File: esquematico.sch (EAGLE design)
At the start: 15 parts, among them IC1 TS321IDBVR, IC2 ESP32-S3-WROOM-1-N16R8, IC3 MAX30102EFD+T

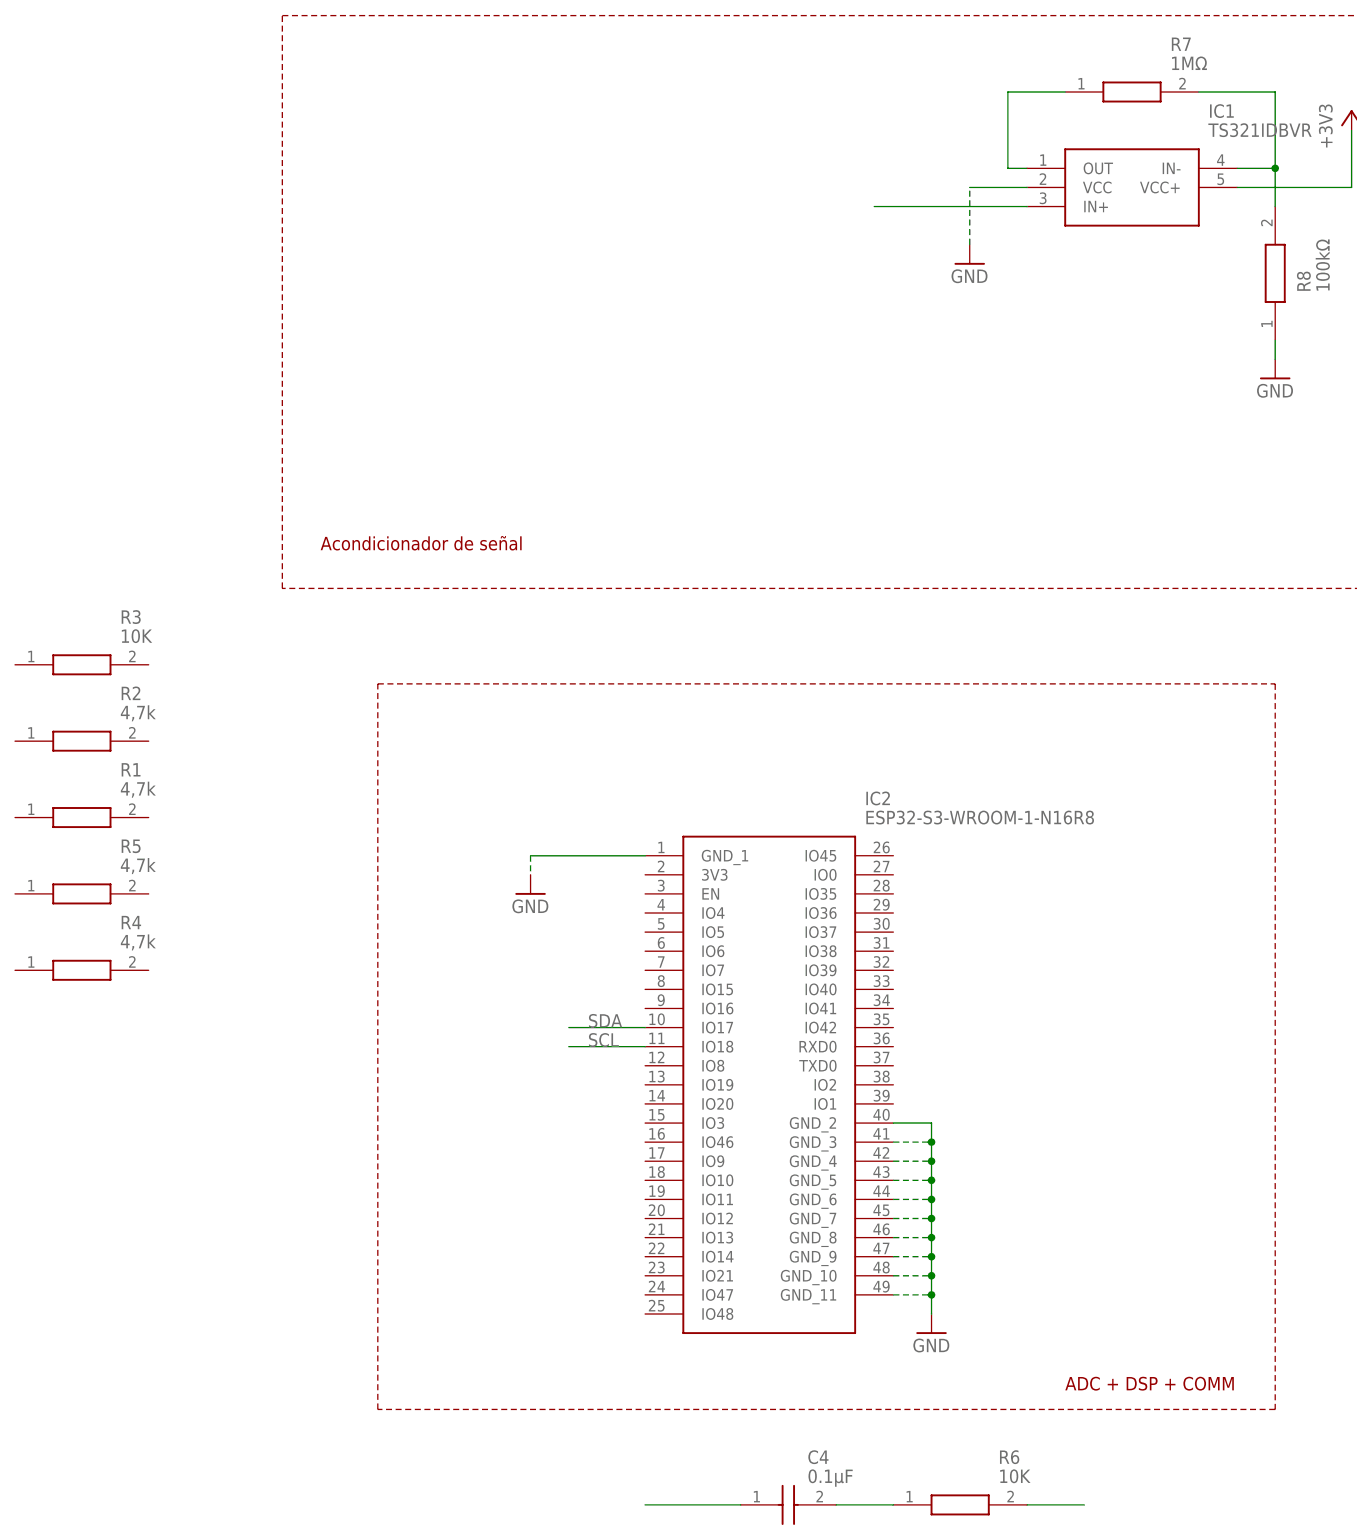
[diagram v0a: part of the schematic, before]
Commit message: Finalizado Bloque 1: Acondicionador de señal
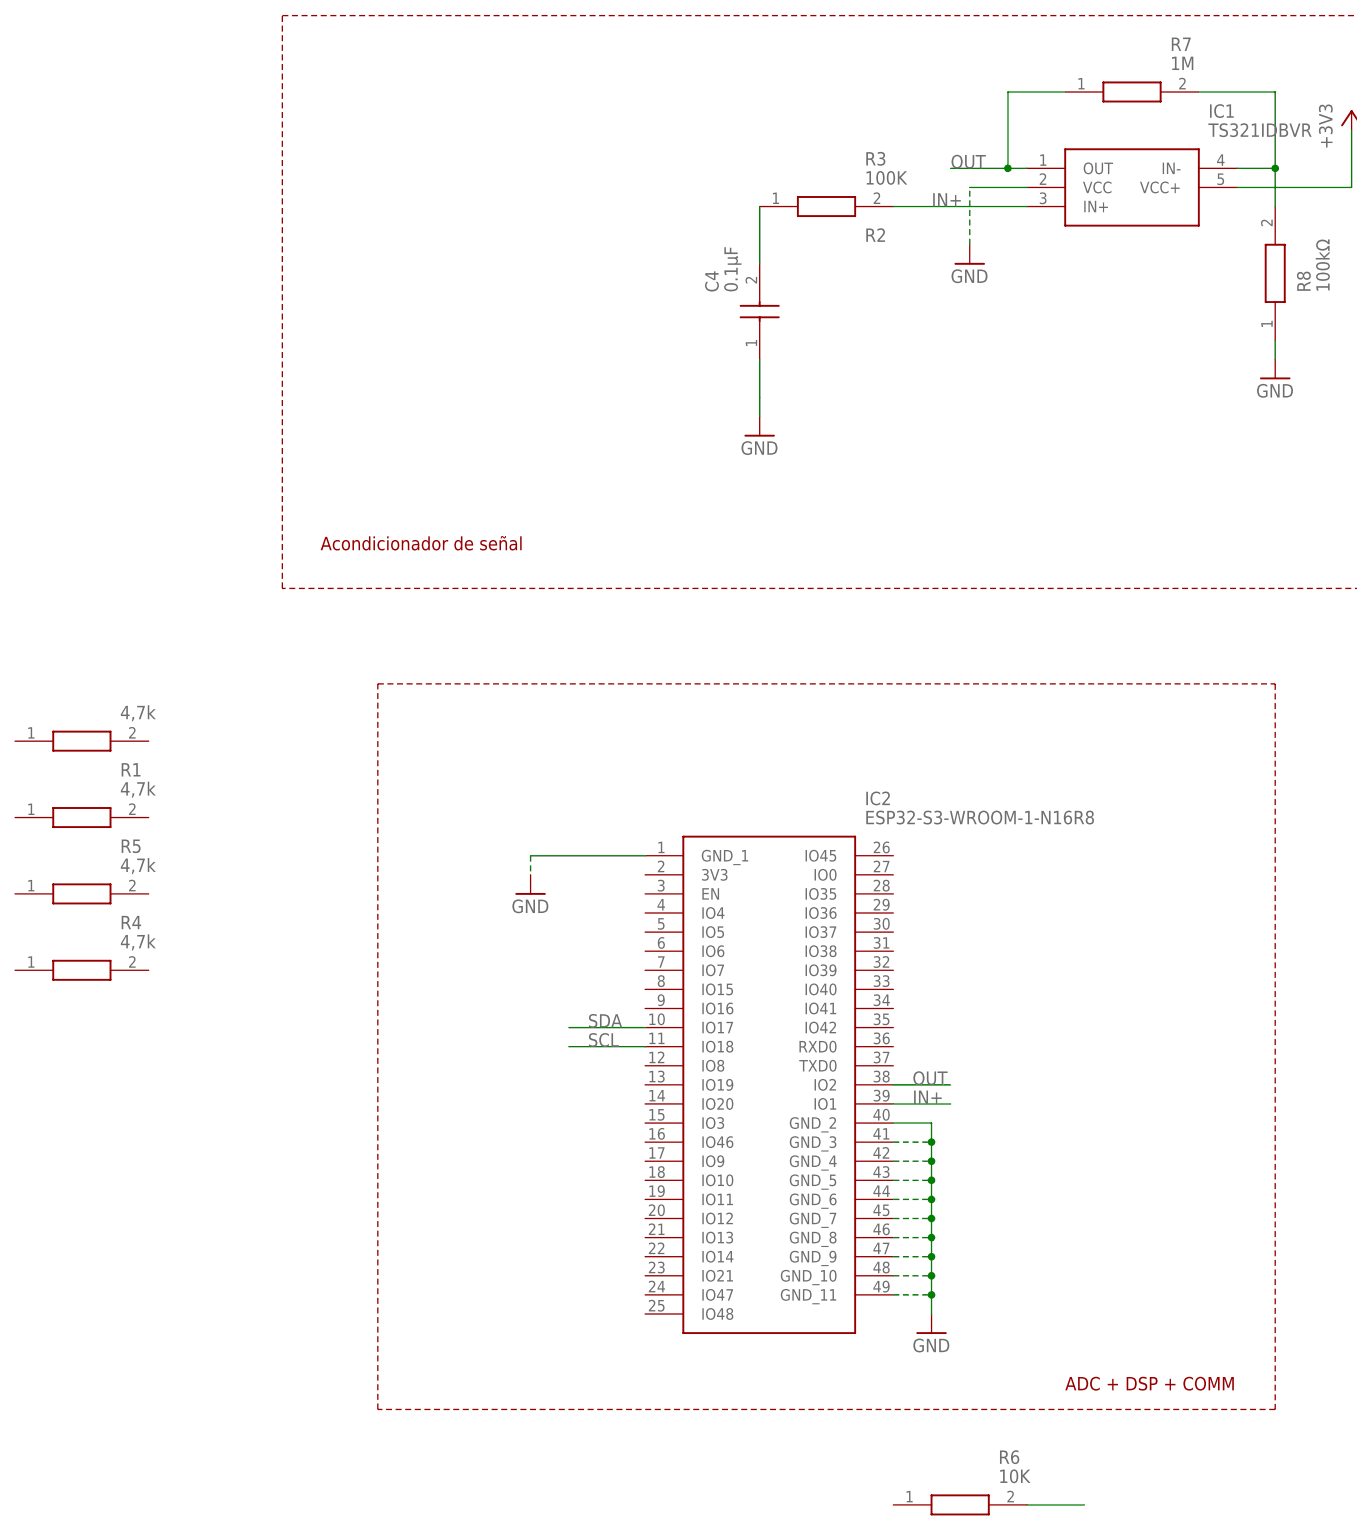
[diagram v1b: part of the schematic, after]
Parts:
- R3: value 10K -> 100K
- R7: value 1MΩ -> 1M
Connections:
- removed net N$11: IC1.IN+
- removed net N$12: C4.2, R6.1
- removed net N$14: IC1.OUT, R7.1
- new net IN+: IC1.IN+, IC2.IO1, R3.2
- new net N$1: C4.2, R3.1
- new net OUT: IC1.OUT, IC2.IO2, R7.1
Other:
- moved on the sheet: C4, R3
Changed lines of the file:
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@@
 <part name="R2" library="0805S8F1202P5E" deviceset="0805S8F1202P5E" device="" value="4,7k"/>
 <part name="R1" library="0805S8F1202P5E" deviceset="0805S8F1202P5E" device="" value="4,7k"/>
-<part name="R3" library="0805S8F1202P5E" deviceset="0805S8F1202P5E" device="" value="10K"/>
+<part name="R3" library="0805S8F1202P5E" deviceset="0805S8F1202P5E" device="" value="100K"/>
 <part name="R4" library="0805S8F1202P5E" deviceset="0805S8F1202P5E" device="" value="4,7k"/>
 <part name="R5" library="0805S8F1202P5E" deviceset="0805S8F1202P5E" device="" value="4,7k"/>
@@
 <part name="R6" library="0805S8F1202P5E" deviceset="0805S8F1202P5E" device="" value="10K"/>
 <part name="C4" library="C0805J104K1RACAUTO" deviceset="C0805J104K1RACAUTO" device="" value="0.1µF"/>
-<part name="R7" library="0805S8F1202P5E" deviceset="0805S8F1202P5E" device="" value="1MΩ"/>
+<part name="R7" library="0805S8F1202P5E" deviceset="0805S8F1202P5E" device="" value="1M"/>
 <part name="R8" library="0805S8F1202P5E" deviceset="0805S8F1202P5E" device="" value="100kΩ"/>
 <part name="+3V1" library="supply1" library_urn="urn:adsk.eagle:library:371" deviceset="+3V3" device=""/>
@@
 <part name="GND6" library="supply1" library_urn="urn:adsk.eagle:library:371" deviceset="GND" device=""/>
 <part name="GND7" library="supply1" library_urn="urn:adsk.eagle:library:371" deviceset="GND" device=""/>
+<part name="GND8" library="supply1" library_urn="urn:adsk.eagle:library:371" deviceset="GND" device=""/>
 </parts>
 <sheets>
@@
 </instance>
 <instance part="R2" gate="G$1" x="76.2" y="142.24" smashed="yes">
-<attribute name="NAME" x="90.17" y="148.59" size="1.778" layer="95" align="center-left"/>
+<attribute name="NAME" x="189.23" y="209.55" size="1.778" layer="95" align="center-left"/>
 <attribute name="VALUE" x="90.17" y="146.05" size="1.778" layer="96" align="center-left"/>
 </instance>
@@
 <attribute name="VALUE" x="90.17" y="135.89" size="1.778" layer="96" align="center-left"/>
 </instance>
-<instance part="R3" gate="G$1" x="76.2" y="152.4" smashed="yes">
-<attribute name="NAME" x="90.17" y="158.75" size="1.778" layer="95" align="center-left"/>
-<attribute name="VALUE" x="90.17" y="156.21" size="1.778" layer="96" align="center-left"/>
+<instance part="R3" gate="G$1" x="175.26" y="213.36" smashed="yes">
+<attribute name="NAME" x="189.23" y="219.71" size="1.778" layer="95" align="center-left"/>
+<attribute name="VALUE" x="189.23" y="217.17" size="1.778" layer="96" align="center-left"/>
 </instance>
 <instance part="R4" gate="G$1" x="76.2" y="111.76" smashed="yes">
@@
 <attribute name="VALUE" x="207.01" y="44.45" size="1.778" layer="96" align="center-left"/>
 </instance>
-<instance part="C4" gate="G$1" x="172.72" y="40.64" smashed="yes">
-<attribute name="NAME" x="181.61" y="46.99" size="1.778" layer="95" align="center-left"/>
-<attribute name="VALUE" x="181.61" y="44.45" size="1.778" layer="96" align="center-left"/>
+<instance part="C4" gate="G$1" x="175.26" y="193.04" smashed="yes" rot="R90">
+<attribute name="NAME" x="168.91" y="201.93" size="1.778" layer="95" rot="R90" align="center-left"/>
+<attribute name="VALUE" x="171.45" y="201.93" size="1.778" layer="96" rot="R90" align="center-left"/>
 </instance>
 <instance part="R7" gate="G$1" x="215.9" y="228.6" smashed="yes">
@@
 <instance part="GND7" gate="1" x="144.78" y="121.92" smashed="yes">
 <attribute name="VALUE" x="142.24" y="119.38" size="1.778" layer="96"/>
+</instance>
+<instance part="GND8" gate="1" x="175.26" y="182.88" smashed="yes">
+<attribute name="VALUE" x="172.72" y="180.34" size="1.778" layer="96"/>
 </instance>
 </instances>
@@
 <pinref part="+3V4" gate="G$1" pin="+3V3"/>
 <wire x1="320.04" y1="134.62" x2="320.04" y2="127" width="0.1524" layer="91"/>
-</segment>
-</net>
-<net name="N$11" class="0">
-<segment>
-<pinref part="IC1" gate="G$1" pin="IN+"/>
-<wire x1="190.5" y1="213.36" x2="210.82" y2="213.36" width="0.1524" layer="91"/>
-</segment>
-</net>
-<net name="N$12" class="0">
-<segment>
-<pinref part="R6" gate="G$1" pin="1"/>
-<pinref part="C4" gate="G$1" pin="2"/>
-<wire x1="185.42" y1="40.64" x2="193.04" y2="40.64" width="0.1524" layer="91"/>
-</segment>
-</net>
-<net name="N$14" class="0">
-<segment>
-<pinref part="IC1" gate="G$1" pin="OUT"/>
-<wire x1="210.82" y1="218.44" x2="208.28" y2="218.44" width="0.1524" layer="91"/>
-<wire x1="208.28" y1="218.44" x2="208.28" y2="228.6" width="0.1524" layer="91"/>
-<wire x1="208.28" y1="228.6" x2="215.9" y2="228.6" width="0.1524" layer="91"/>
-<pinref part="R7" gate="G$1" pin="1"/>
 </segment>
 </net>
@@
 <wire x1="144.78" y1="127" x2="144.78" y2="124.46" width="0.1524" layer="91" style="longdash"/>
 </segment>
+<segment>
+<pinref part="GND8" gate="1" pin="GND"/>
+<wire x1="175.26" y1="187.96" x2="175.26" y2="185.42" width="0.1524" layer="91"/>
+</segment>
 </net>
 <net name="N$10" class="0">
@@
 </segment>
 </net>
-<net name="N$17" class="0">
-<segment>
-<pinref part="C4" gate="G$1" pin="1"/>
-<wire x1="172.72" y1="40.64" x2="160.02" y2="40.64" width="0.1524" layer="91"/>
-</segment>
-</net>
 <net name="N$13" class="0">
 <segment>
@@
 </segment>
 </net>
+<net name="IN+" class="0">
+<segment>
+<pinref part="IC2" gate="G$1" pin="IO1"/>
+<wire x1="193.04" y1="93.98" x2="200.66" y2="93.98" width="0.1524" layer="91"/>
+<label x="195.58" y="93.98" size="1.778" layer="95"/>
+</segment>
+<segment>
+<pinref part="IC1" gate="G$1" pin="IN+"/>
+<wire x1="193.04" y1="213.36" x2="210.82" y2="213.36" width="0.1524" layer="91"/>
+<label x="198.12" y="213.36" size="1.778" layer="95"/>
+<pinref part="R3" gate="G$1" pin="2"/>
+</segment>
+</net>
+<net name="N$1" class="0">
+<segment>
+<pinref part="R3" gate="G$1" pin="1"/>
+<pinref part="C4" gate="G$1" pin="2"/>
+<wire x1="175.26" y1="213.36" x2="175.26" y2="205.74" width="0.1524" layer="91"/>
+</segment>
+</net>
+<net name="N$2" class="0">
+<segment>
+<pinref part="C4" gate="G$1" pin="1"/>
+<wire x1="175.26" y1="193.04" x2="175.26" y2="187.96" width="0.1524" layer="91"/>
+</segment>
+</net>
+<net name="OUT" class="0">
+<segment>
+<pinref part="IC2" gate="G$1" pin="IO2"/>
+<wire x1="193.04" y1="96.52" x2="200.66" y2="96.52" width="0.1524" layer="91"/>
+<label x="195.58" y="96.52" size="1.778" layer="95"/>
+</segment>
+<segment>
+<pinref part="IC1" gate="G$1" pin="OUT"/>
+<wire x1="210.82" y1="218.44" x2="208.28" y2="218.44" width="0.1524" layer="91"/>
+<wire x1="208.28" y1="218.44" x2="208.28" y2="228.6" width="0.1524" layer="91"/>
+<wire x1="208.28" y1="228.6" x2="215.9" y2="228.6" width="0.1524" layer="91"/>
+<pinref part="R7" gate="G$1" pin="1"/>
+<wire x1="208.28" y1="218.44" x2="200.66" y2="218.44" width="0.1524" layer="91"/>
+<junction x="208.28" y="218.44"/>
+<label x="200.66" y="218.44" size="1.778" layer="95"/>
+</segment>
+</net>
